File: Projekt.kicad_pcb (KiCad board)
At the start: 2 copper layers, 93 parts, among them J1 Solar, J2 Battery, J3 USB_B_Mini, J4 INTERFACE PORT, J5 FAN, Q1 CSD19505KCS, Q2 CSD19505KCS, Q3 CSD19505KCS, Q4 Si2306, Q5 MMBT3904 1A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

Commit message: So gut wie fertig ... ?
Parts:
- added J6: JTAG, Connector_PinHeader_1.27mm:PinHeader_2x05_P1.27mm_Vertical_SMD, F.Cu at (136.0, 121.5)
- added REF**: MountingHole_3.2mm_M3, MountingHole:MountingHole_3.2mm_M3, F.Cu at (82.0, 97.0)
- added REF**: MountingHole_3.2mm_M3, MountingHole:MountingHole_3.2mm_M3, F.Cu at (81.5, 151.5)
- added REF**: MountingHole_3.2mm_M3, MountingHole:MountingHole_3.2mm_M3, F.Cu at (158.5, 97.5)
- added REF**: MountingHole_3.2mm_M3, MountingHole:MountingHole_3.2mm_M3, F.Cu at (158.5, 151.5)
- D1, D3, D6, R17, R19, R4, U3, U5, U6: moved to F.Cu
- D4: footprint Diode_SMD:D_SMC -> Diode_SMD:D_SMB; moved to B.Cu
- D5, D7, U10: moved to B.Cu
- D8: footprint Diode_SMD:D_SMC -> Diode_SMD:D_SMB
- moved C5 89.4 mm to (110.3, 114.0), turned to 0 degrees
- moved D7 88.1 mm to (135.7, 140.6)
- moved C6 85.7 mm to (110.4, 116.6)
- moved D6 75.1 mm to (125.4, 135.5), turned to 90 degrees
- moved U3 72.8 mm to (117.3, 103.9), turned to 0 degrees
- moved U6 62.5 mm to (123.0, 118.5), turned to 0 degrees
- moved L3 59.7 mm to (135.3, 113.5)
- moved R25 59.5 mm to (139.6, 144.4)
- moved C12 58.8 mm to (138.1, 119.5)
- moved C15 58.3 mm to (133.5, 126.0), turned to 0 degrees
- moved R1 57.2 mm to (133.8, 143.8)
- moved R24 56.9 mm to (155.5, 142.0)
- moved C17 55.7 mm to (135.5, 110.3)
- moved R12 55.0 mm to (131.4, 114.8), turned to 180 degrees
- moved R18 54.6 mm to (136.1, 114.9), turned to 180 degrees
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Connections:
- C1 pad 2: GND -> unconnected-(C1-Pad2)
- J4 pad 2: +3.3V -> +5V
- U8 pad 13: unconnected-(U8-Pad13) -> Net-(U8-Pad13)
- U8 pad 14: unconnected-(U8-Pad14) -> Net-(U8-Pad14)
- U8 pad 16: unconnected-(U8-Pad16) -> Net-(U8-Pad16)
- U8 pad 23: unconnected-(U8-Pad23) -> Net-(U8-Pad23)
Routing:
- net GND: track 22.4 -> 89.6 mm
- net Net-(C10-Pad2): track 0.00 -> 39.3 mm
- net Net-(D4-Pad2): track 0.00 -> 26.9 mm
- net Net-(C4-Pad2): track 0.00 -> 26.9 mm
- net Net-(C8-Pad1): track 0.00 -> 25.2 mm
- net Net-(D8-Pad2): track 0.00 -> 24.0 mm
- net Net-(Q1-Pad2): track 0.00 -> 21.3 mm
- net Net-(C7-Pad1): track 0.00 -> 17.2 mm
- net Net-(C21-Pad1): track 14.4 -> 0.00 mm, vias 1 -> 0
- net Net-(C22-Pad1): track 2.81 -> 0.00 mm
- net Net-(C3-Pad2): track 2.75 -> 0.00 mm
- net (no net): track 2.55 -> 0.00 mm
- removed copper zone on B.Cu, net Net-(D8-Pad2)
- removed copper zone on F.Cu, net Net-(D8-Pad2)
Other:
- board outline added: 83.2 x 60.8 mm

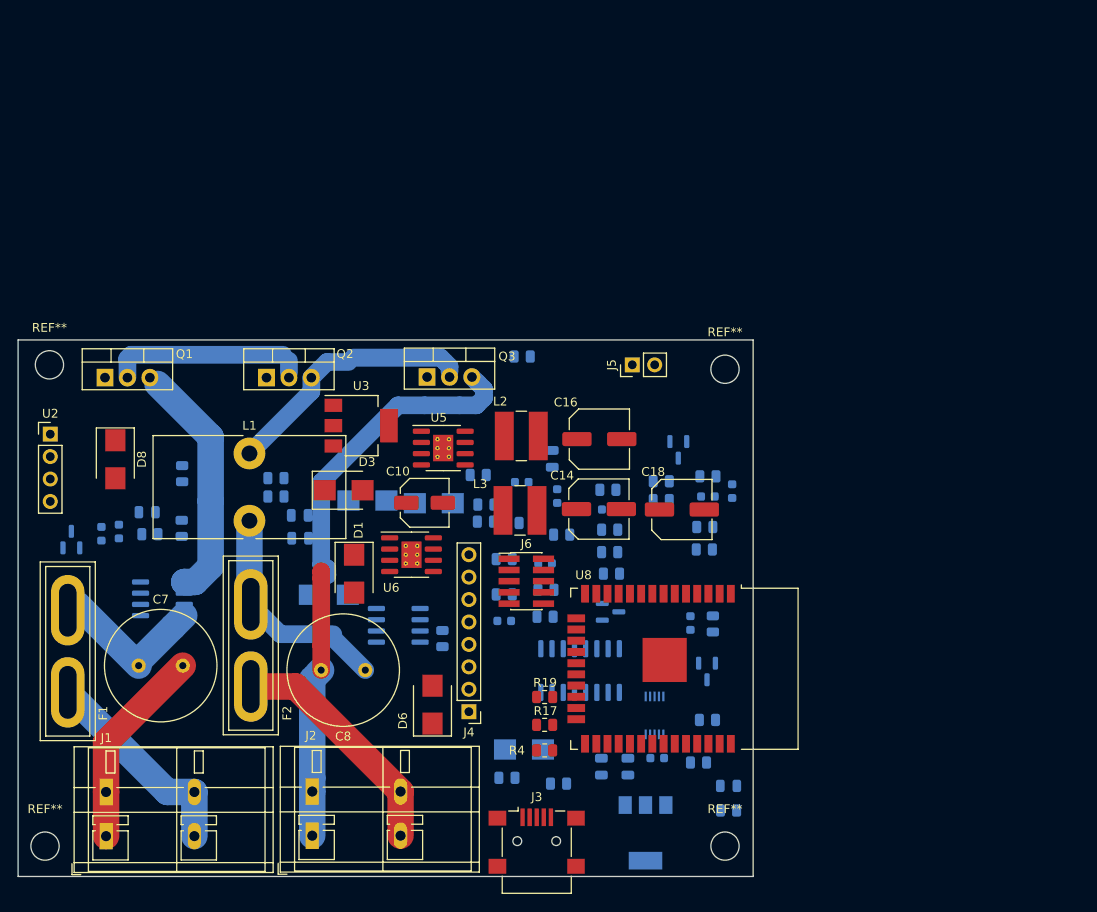
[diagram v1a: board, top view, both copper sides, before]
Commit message: Leiterbahnen verstärkt
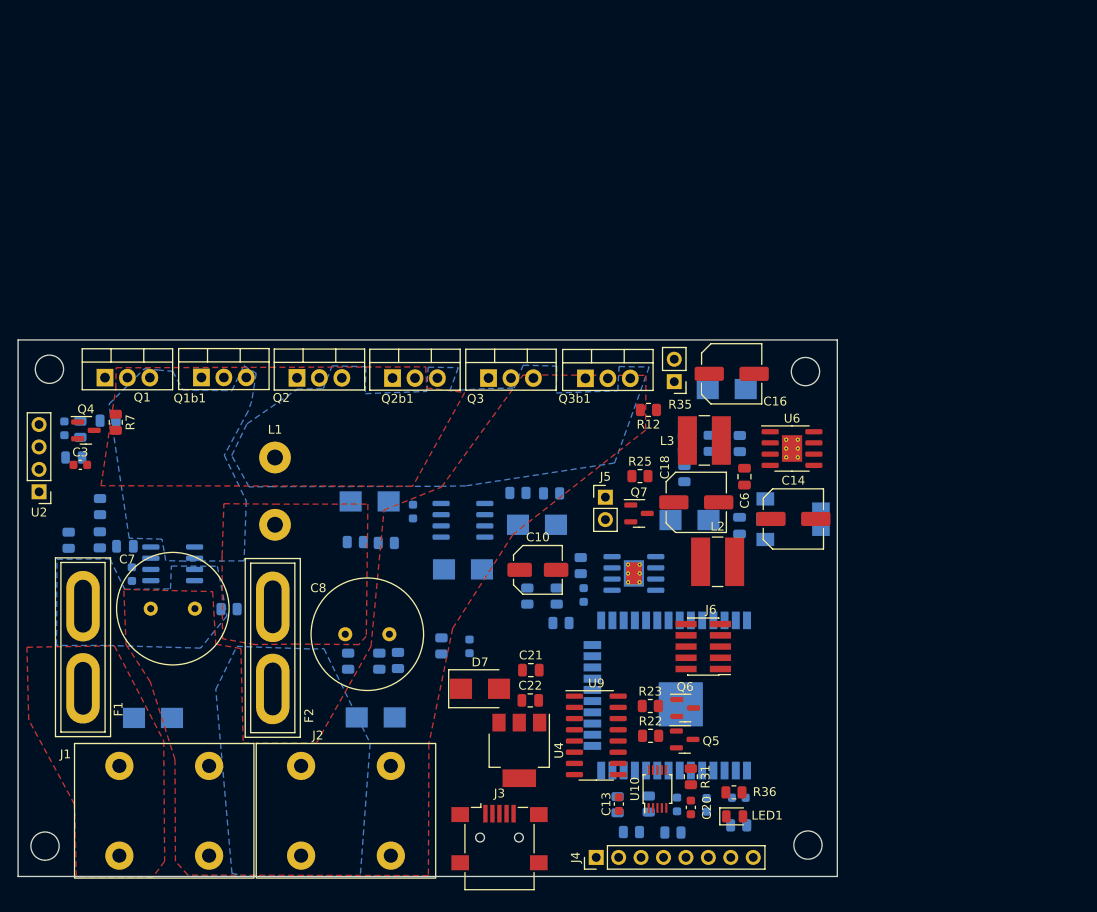
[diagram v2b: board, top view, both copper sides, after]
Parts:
- added C11: 100nF, Capacitor_SMD:C_0603_1608Metric, B.Cu at (123.2, 113.6)
- added Q1b1: CSD19505KCS, Package_TO_SOT_THT:TO-220-3_Vertical, F.Cu at (99.2, 98.4)
- added Q2b1: CSD19505KCS, Package_TO_SOT_THT:TO-220-3_Vertical, F.Cu at (120.9, 98.5)
- added Q3b1: CSD19505KCS, Package_TO_SOT_THT:TO-220-3_Vertical, F.Cu at (142.7, 98.5)
- C13, C20, C21, C22, C3, C6, D7, LED1, Q4, Q5, Q6, Q7, R12, R22, R23, R25, R31, R36, R7, U10, U4, U9: moved to F.Cu
- D1, D3, D6, D8, R17, R19, R4, U3, U5, U8: moved to B.Cu
- J1, J2: footprint TerminalBlock_WAGO:TerminalBlock_WAGO_236-602_1x02_P10.00mm_45Degree -> footprints:TerminalBlock_DEGSON_DG135T
- R35: footprint Resistor_SMD:R_0805_2012Metric -> Connector_PinHeader_2.54mm:PinHeader_1x02_P2.54mm_Vertical; moved to F.Cu
- moved R3 63.7 mm to (87.7, 116.8), turned to 90 degrees
- moved R5 63.6 mm to (87.7, 113.1), turned to -90 degrees
- moved R4 58.9 mm to (84.2, 116.9), turned to -90 degrees
- moved C6 50.8 mm to (160.7, 109.7), turned to 90 degrees
- moved U3 50.1 mm to (166.2, 114.5)
- moved C5 49.8 mm to (160.1, 115.2), turned to -90 degrees
- moved C9 49.4 mm to (90.6, 117.6), turned to 180 degrees
- moved C2 49.0 mm to (91.3, 120.7)
- moved D6 48.9 mm to (158.7, 99.7), turned to 180 degrees
- moved U6 44.7 mm to (166.1, 106.5)
- moved R21 39.7 mm to (160.1, 149.1)
- moved R17 37.0 mm to (156.8, 105.9), turned to -90 degrees
- moved R1 36.8 mm to (102.3, 124.7)
- moved D5 36.5 mm to (154.5, 114.6)
- moved R25 36.0 mm to (148.9, 109.6), turned to 0 degrees
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- renumbered REF** to REF1, REF** to REF2, REF** to REF3, REF** to REF4
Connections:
- J1 pad 1: GND -> Net-(D8-Pad2)
- J1 pad 2: Net-(D8-Pad2) -> GND
- J2 pad 1: GND -> Net-(D4-Pad2)
- J2 pad 2: Net-(D4-Pad2) -> GND
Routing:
- net GND: track 89.6 -> 0.00 mm
- net Net-(C10-Pad2): track 39.3 -> 0.00 mm
- net Net-(D4-Pad2): track 26.9 -> 0.00 mm
- net Net-(C4-Pad2): track 26.9 -> 0.00 mm
- net Net-(C8-Pad1): track 25.2 -> 0.00 mm
- net Net-(D8-Pad2): track 24.0 -> 0.00 mm
- net Net-(Q1-Pad2): track 21.3 -> 0.00 mm
- net Net-(C7-Pad1): track 17.2 -> 0.00 mm
- added copper zone on F.Cu, net GND
- added copper zone on B.Cu, net Net-(C10-Pad2)
- added copper zone on B.Cu, net Net-(C4-Pad2)
- added copper zone on B.Cu, net Net-(C7-Pad1)
- added copper zone on F.Cu, net Net-(C8-Pad1)
- added copper zone on B.Cu, net Net-(D4-Pad2)
- added copper zone on F.Cu, net Net-(D8-Pad2)
- added copper zone on F.Cu, net Net-(Q1-Pad2)
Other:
- board size 83.2 x 60.8 mm -> 92.8 x 60.8 mm

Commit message: Eigentlich okay...
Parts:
- removed Q1b1, Q2b1, Q3b1: CSD19505KCS, Package_TO_SOT_THT:TO-220-3_Vertical
- added ?: , , F.Cu at (110.0, 107.4)
- added ?: , , F.Cu at (110.0, 115.1)
- added J7: PRG, Connector_PinHeader_2.54mm:PinHeader_1x02_P2.54mm_Vertical, F.Cu at (137.0, 128.7)
- added Q11: CSD19505KCS, Package_TO_SOT_THT:TO-220-3_Vertical, F.Cu at (99.1, 98.5)
- added Q12: CSD19505KCS, Package_TO_SOT_THT:TO-220-3_Vertical, F.Cu at (120.9, 98.5)
- added Q13: CSD19505KCS, Package_TO_SOT_THT:TO-220-3_Vertical, F.Cu at (142.7, 98.5)
- C11, D2, D3, D4, D8, R10, R11, U7: moved to F.Cu
- moved D8 41.1 mm to (125.3, 110.6), turned to -90 degrees
- moved R1 25.4 mm to (127.4, 129.0), turned to 90 degrees
- moved R32 21.4 mm to (136.2, 137.0), turned to 0 degrees
- moved R33 17.4 mm to (136.2, 134.7), turned to 0 degrees
- moved D2 15.5 mm to (130.6, 121.8), turned to 90 degrees
- moved R34 14.9 mm to (136.2, 132.6), turned to 180 degrees
- moved C9 14.3 mm to (79.8, 127.0), turned to -90 degrees
- moved C2 11.6 mm to (79.8, 120.1)
- moved R11 11.4 mm to (126.0, 123.4), turned to -90 degrees
- moved U1 11.1 mm to (85.2, 116.8)
- moved R3 10.4 mm to (79.8, 123.4), turned to -90 degrees
- moved D4 10.2 mm to (128.5, 140.5), turned to -90 degrees
- moved D3 9.91 mm to (130.7, 110.4), turned to 90 degrees
- moved U7 9.69 mm to (137.9, 111.2), turned to 90 degrees
- moved C11 7.14 mm to (129.5, 116.9), turned to 0 degrees
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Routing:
- net GND: track 0.00 -> 534.7 mm
- net Net-(D8-Pad2): track 0.00 -> 388.6 mm
- net Net-(C8-Pad1): track 0.00 -> 334.1 mm
- net Net-(C7-Pad1): track 0.00 -> 229.1 mm, vias 0 -> 6
- net Net-(D4-Pad2): track 0.00 -> 196.7 mm
- net Net-(C10-Pad2): track 0.00 -> 190.3 mm
- net Net-(C4-Pad2): track 0.00 -> 147.6 mm
- net Net-(Q1-Pad2): track 0.00 -> 42.5 mm
- removed copper zone on F.Cu, net GND
- removed copper zone on B.Cu, net Net-(C10-Pad2)
- removed copper zone on B.Cu, net Net-(C4-Pad2)
- removed copper zone on B.Cu, net Net-(C7-Pad1)
- removed copper zone on F.Cu, net Net-(C8-Pad1)
- removed copper zone on B.Cu, net Net-(D4-Pad2)
- removed copper zone on F.Cu, net Net-(D8-Pad2)
- removed copper zone on F.Cu, net Net-(Q1-Pad2)
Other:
- board text added: "JTAG"

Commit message: Fehlerhafte Pads entfernt und in Footprint eingebaut
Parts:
- removed ? (x2): , 
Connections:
- C1 pad 2: unconnected-(C1-Pad2) -> GND
- J7 pad 1: GND -> GPIO0
- J7 pad 2: GPIO0 -> GND

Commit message: Jaaa
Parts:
- C4, R37, R5: moved to F.Cu
- moved R3 14.2 mm to (83.8, 109.9), turned to 90 degrees
- moved C9 11.8 mm to (80.4, 115.3), turned to 90 degrees
- moved R4 9.64 mm to (83.8, 106.1), turned to 90 degrees
- moved LED2 7.54 mm to (90.2, 102.2), turned to 180 degrees
- moved R5 6.26 mm to (86.4, 106.7), turned to 90 degrees
- moved R37 5.68 mm to (83.8, 106.3), turned to -90 degrees
- moved R7 4.80 mm to (89.5, 108.3)
- moved Q4 3.85 mm to (89.9, 103.5)
- moved C4 3.01 mm to (86.4, 102.9)
- moved C3 2.33 mm to (86.4, 110.5), turned to 90 degrees
- moved R6 2.23 mm to (86.4, 102.2), turned to 0 degrees
- moved C2 1.78 mm to (80.6, 118.6)
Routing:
- net GND: track 534.7 -> 1060.8 mm, vias 0 -> 12
- net +5V: track 0.00 -> 212.4 mm, vias 0 -> 4
- net +12V: track 0.00 -> 201.1 mm, vias 0 -> 5
- net +3.3V: track 0.00 -> 170.2 mm, vias 0 -> 9
- net Net-(C18-Pad1): track 0.00 -> 116.4 mm, vias 0 -> 5
- net GPIO27: track 0.00 -> 112.2 mm, vias 0 -> 5
- net A2: track 0.00 -> 108.6 mm, vias 0 -> 6
- net GPIO33: track 0.00 -> 107.3 mm, vias 0 -> 7
- net Net-(C4-Pad1): track 0.00 -> 107.0 mm, vias 0 -> 4
- net Net-(D8-Pad2): track 388.6 -> 469.6 mm, vias 0 -> 2
- net Net-(LED1-Pad2): track 0.00 -> 80.0 mm, vias 0 -> 9
- net SDA: track 0.00 -> 77.2 mm, vias 0 -> 1
- net Net-(C12-Pad1): track 0.00 -> 70.8 mm, vias 0 -> 4
- net GPIO32: track 0.00 -> 64.8 mm, vias 0 -> 1
- net Net-(C7-Pad1): track 229.1 -> 289.1 mm, vias 6 -> 1
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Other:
- board text added: "TODO: GND Q3 Q13"

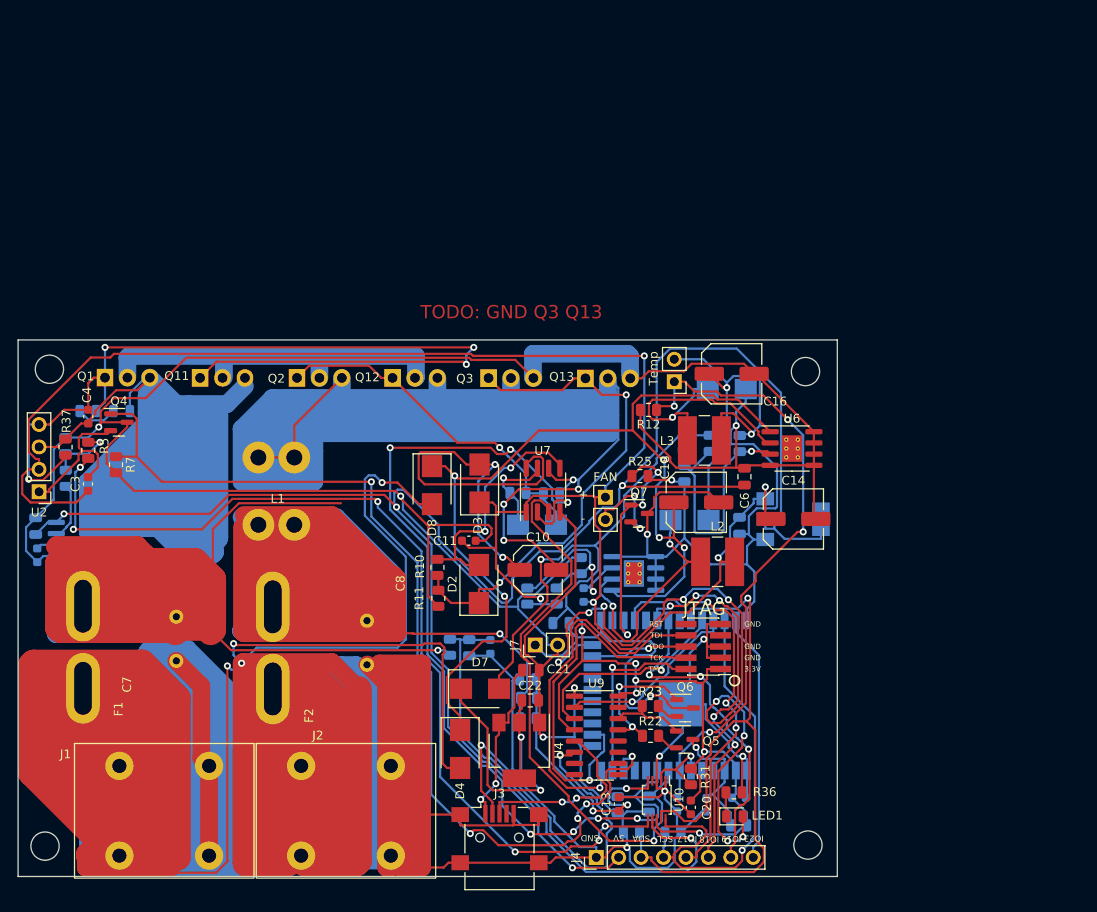
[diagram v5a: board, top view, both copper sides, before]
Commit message: SD + RTC
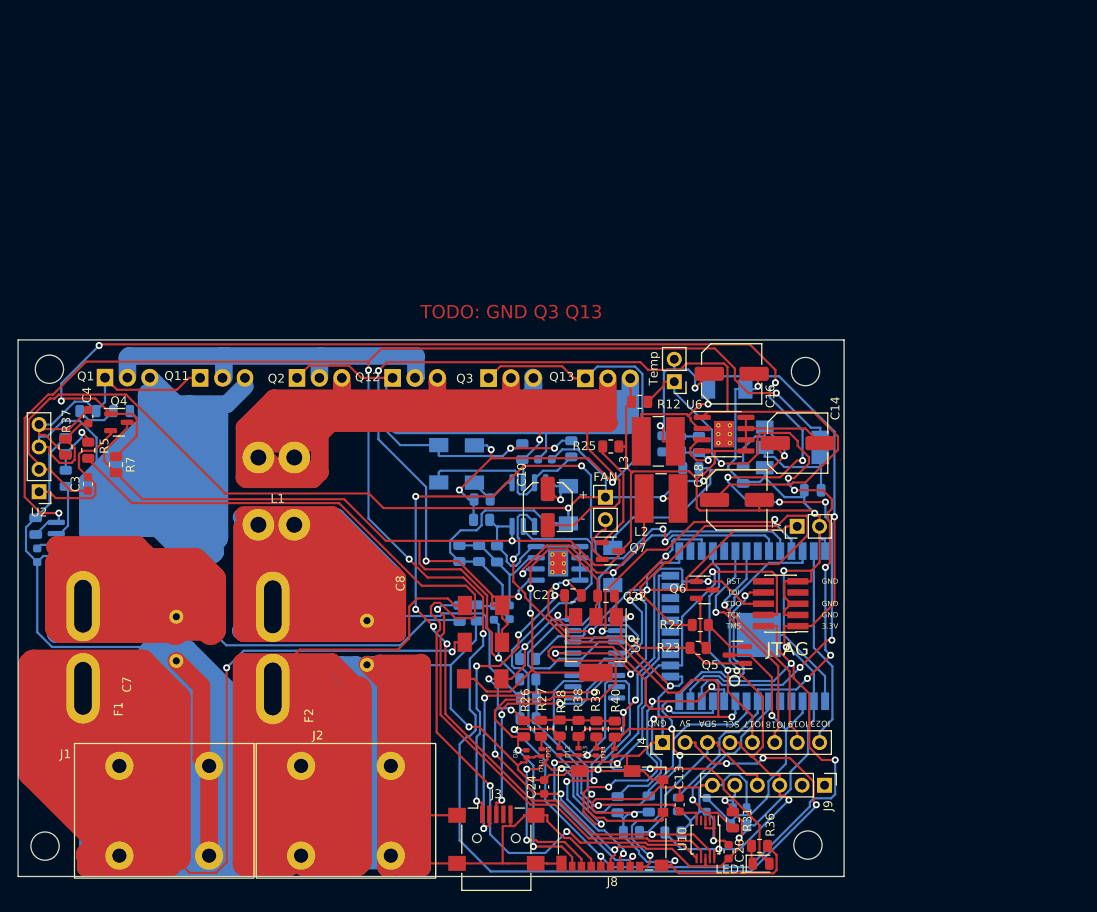
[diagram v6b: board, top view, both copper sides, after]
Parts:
- added C24: 100nF, Capacitor_SMD:C_0603_1608Metric, F.Cu at (138.0, 144.8)
- added D10: LESD8D3.3CAT5G, AA:SOD882D.kicad_mod, F.Cu at (137.7, 140.9)
- added D11: LESD8D3.3CAT5G, AA:SOD882D.kicad_mod, F.Cu at (139.8, 140.8)
- added D12: LESD8D3.3CAT5G, AA:SOD882D.kicad_mod, F.Cu at (141.9, 140.8)
- added D13: LESD8D3.3CAT5G, AA:SOD882D.kicad_mod, F.Cu at (143.9, 140.8)
- added D14: LESD8D3.3CAT5G, AA:SOD882D.kicad_mod, F.Cu at (146.0, 140.9)
- added D9: LESD8D3.3CAT5G, AA:SOD882D.kicad_mod, F.Cu at (136.0, 141.0)
- added J8: Micro_SD_Card_Det_Hirose_DM3AT, AA:microSD_HC_Molex_104031-0811, F.Cu at (145.7, 148.4)
- added J9: IIC RTC, Connector_PinHeader_2.54mm:PinHeader_1x06_P2.54mm_Vertical, F.Cu at (169.8, 144.6)
- added R26: 10k, Resistor_SMD:R_0805_2012Metric, F.Cu at (135.7, 138.2)
- added R27: 10k, Resistor_SMD:R_0805_2012Metric, F.Cu at (137.7, 138.2)
- added R28: 10k, Resistor_SMD:R_0805_2012Metric, F.Cu at (139.8, 138.1)
- added R38: 10k, Resistor_SMD:R_0805_2012Metric, F.Cu at (141.9, 138.2)
- added R39: 10k, Resistor_SMD:R_0805_2012Metric, F.Cu at (143.9, 138.2)
- added R40: 10k, Resistor_SMD:R_0805_2012Metric, F.Cu at (146.0, 138.3)
- C11, C6, R10, R11, U7, U9: moved to B.Cu
- D1, D4, D5, D6, D7, D8: footprint Diode_SMD:D_SMB -> AA:DO-214AA
- D2, D3: footprint Diode_SMD:D_SMB -> AA:DO-214AA; moved to B.Cu
- moved J7 32.6 mm to (166.7, 115.3)
- moved D8 18.7 mm to (131.1, 128.4), turned to 180 degrees
- moved D4 16.5 mm to (131.2, 124.3), turned to 180 degrees
- moved J4 15.0 mm to (151.4, 139.8)
- moved U4 14.8 mm to (143.9, 128.7)
- moved C22 14.6 mm to (145.0, 123.2)
- moved R22 13.8 mm to (155.7, 126.5)
- moved D2 13.6 mm to (130.1, 108.2), turned to -90 degrees
- moved Q6 13.6 mm to (156.2, 122.5)
- moved D1 13.1 mm to (126.1, 108.2), turned to -90 degrees
- moved C11 12.6 mm to (138.1, 107.7), turned to 180 degrees
- moved U8 11.8 mm to (161.6, 126.6)
- moved Q5 11.3 mm to (159.9, 129.9), turned to 180 degrees
- moved D3 10.3 mm to (140.8, 112.9)
- moved D5 10.2 mm to (145.8, 119.8), turned to -90 degrees
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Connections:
- net Net-(J6-Pad2) renamed GPIO14
- net Net-(J6-Pad4) renamed GPIO13
- net Net-(J6-Pad6) renamed GPIO15
- net Net-(J6-Pad8) renamed GPIO12
- U8 pad 10: unconnected-(U8-Pad10) -> GPIO25
- U8 pad 11: unconnected-(U8-Pad11) -> GPIO26
- U8 pad 27: Net-(Q7-Pad1) -> GPIO16
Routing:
- net GND: track 1060.8 -> 1157.4 mm, vias 12 -> 15
- net GPIO26: track 0.00 -> 76.0 mm, vias 0 -> 3
- net GPIO14: track 20.7 -> 95.8 mm, vias 1 -> 4
- net Net-(C4-Pad1): track 107.0 -> 35.7 mm, vias 4 -> 0
- net GPIO25: track 0.00 -> 65.7 mm, vias 0 -> 7
- net SDA: track 77.2 -> 141.5 mm, vias 1 -> 8
- net GPIO27: track 112.2 -> 169.5 mm, vias 5 -> 9
- net GPIO15: track 11.1 -> 67.9 mm, vias 1 -> 6
- net GPIO16: track 0.00 -> 56.4 mm, vias 0 -> 3
- net Net-(Q6-Pad1): track 15.6 -> 69.3 mm, vias 2 -> 3
- net +5V: track 212.4 -> 259.1 mm, vias 4 -> 8
- net Net-(C10-Pad2): track 248.4 -> 204.6 mm, vias 4 -> 1
- net Net-(C10-Pad1): track 46.7 -> 6.29 mm, vias 2 -> 1
- net GPIO33: track 107.3 -> 67.1 mm, vias 7 -> 3
- net +12V: track 201.1 -> 162.7 mm, vias 5 -> 4
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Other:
- board size 92.8 x 60.8 mm -> 93.5 x 60.8 mm

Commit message: RC1
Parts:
- LED2, R6: moved to F.Cu
- U6: moved to B.Cu
- moved R13 36.5 mm to (132.3, 113.1)
- moved R20 32.1 mm to (134.8, 118.4)
- moved L2 20.1 mm to (132.2, 118.4)
- moved C14 16.6 mm to (151.4, 112.1)
- moved R21 15.5 mm to (168.2, 136.0)
- moved R30 14.9 mm to (154.6, 136.6)
- moved R29 14.5 mm to (158.2, 136.6), turned to 0 degrees
- moved C12 13.4 mm to (161.6, 136.4), turned to 180 degrees
- moved C19 13.4 mm to (164.9, 136.5), turned to 0 degrees
- moved C23 12.5 mm to (168.5, 137.8)
- moved R25 12.2 mm to (142.6, 118.1), turned to -90 degrees
- moved C16 10.3 mm to (166.9, 104.9)
- moved LED2 9.63 mm to (80.5, 101.9), turned to 0 degrees
- moved C11 7.98 mm to (137.8, 115.7)
- moved R10 5.76 mm to (132.6, 106.7), turned to 90 degrees
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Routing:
- net GND: track 1157.4 -> 1072.6 mm, vias 15 -> 13
- net +5V: track 259.1 -> 176.1 mm, vias 8 -> 1
- net Net-(C18-Pad1): track 126.5 -> 53.7 mm, vias 3 -> 2
- net SDA: track 141.5 -> 69.7 mm, vias 8 -> 1
- net GPIO27: track 169.5 -> 98.2 mm, vias 9 -> 3
- net Net-(Q6-Pad1): track 69.3 -> 20.3 mm, vias 3 -> 1
- net GPIO14: track 95.8 -> 53.7 mm, vias 4 -> 3
- net Net-(C12-Pad1): track 84.9 -> 56.2 mm, vias 6 -> 2
- net GPIO32: track 73.4 -> 47.7 mm, vias 0 -> 2
- net +12V: track 162.7 -> 137.6 mm, vias 4 -> 2
- net GPIO25: track 65.7 -> 42.4 mm, vias 7 -> 4
- net Net-(C22-Pad1): track 42.5 -> 20.2 mm, vias 2 -> 0
- net RX: track 50.8 -> 29.5 mm
- net EN: track 34.6 -> 14.9 mm
- net GPIO26: track 76.0 -> 56.3 mm, vias 3 -> 6
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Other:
- board text added: "<- GND CU BAR ->"
- board text added: "Bat."
- board text added: "GND"
- board text added: "Solar"
- board text removed: "TODO: GND Q3 Q13"
